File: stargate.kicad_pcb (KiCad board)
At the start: 2 copper layers, 96 x 65.5 mm, 32 parts, among them J1 Mot_Conn, J10 Chev5_conn, J11 Chev6_conn, J12 Chev7_conn, J13 Audio_conn, J14 IOExpander_Conn, J2 Power_Conn, J3 LED_Strip_Conn, J4 DHD_Conn, J5 Level_Converter, J6 Chev1_conn, J7 Chev2_conn, J8 Chev3_conn, J9 Chev4_conn, Q1 PN2222A, Q2 PN2222A, Q3 PN2222A, Q4 PN2222A, Q5 PN2222A, Q6 PN2222A, Q7 PN2222A, U1 ESP32-S3-DevKitC

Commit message: Updates
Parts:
- removed Q1, Q2, Q3, Q4, Q5, Q6, Q7: PN2222A, Package_TO_SOT_THT:TO-92_Inline
- removed R2, R3, R4, R5, R6, R7, R8: 220Ω, Resistor_THT:R_Axial_DIN0204_L3.6mm_D1.6mm_P7.62mm_Horizontal
- added U2: ULN2803A, Package_DIP:DIP-18_W7.62mm, F.Cu at (91.8, 71.9)
- moved J12 54.6 mm to (68.9, 92.2)
- moved J6 53.7 mm to (123.2, 92.2)
- moved J11 36.6 mm to (77.9, 92.2)
- moved J7 35.5 mm to (113.9, 92.2)
- moved J10 18.6 mm to (86.9, 92.2)
- moved J8 17.5 mm to (104.9, 92.2)
- moved J9 1.45 mm to (95.9, 92.2)
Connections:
- U1 pad 1: 3V3 -> unconnected-(U1-3V3-Pad1)
- U1 pad 2: 3V3 -> unconnected-(U1-3V3-Pad1)
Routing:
- net Net-(Q7-B): track 48.3 -> 0.00 mm, vias 2 -> 0
- net Net-(Q6-B): track 38.9 -> 0.00 mm, vias 2 -> 0
- net Net-(Q1-B): track 34.6 -> 0.00 mm
- net Net-(Q5-B): track 31.5 -> 0.00 mm, vias 2 -> 0
- net Net-(J6-Pin_1): track 7.00 -> 36.6 mm
- net Chev1_led: track 42.2 -> 69.1 mm
- net Net-(Q2-B): track 26.9 -> 0.00 mm
- net Net-(Q3-B): track 25.2 -> 0.00 mm
- net Net-(Q4-B): track 24.9 -> 0.00 mm
- net Net-(J7-Pin_1): track 7.00 -> 29.9 mm
- net Chev2_led: track 42.8 -> 65.5 mm
- net 3V3: track 230.9 -> 209.8 mm, vias 2 -> 0
- net Chev3_led: track 43.4 -> 61.9 mm
- net Net-(J8-Pin_1): track 7.00 -> 23.5 mm
- net Chev4_led: track 39.8 -> 54.1 mm
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
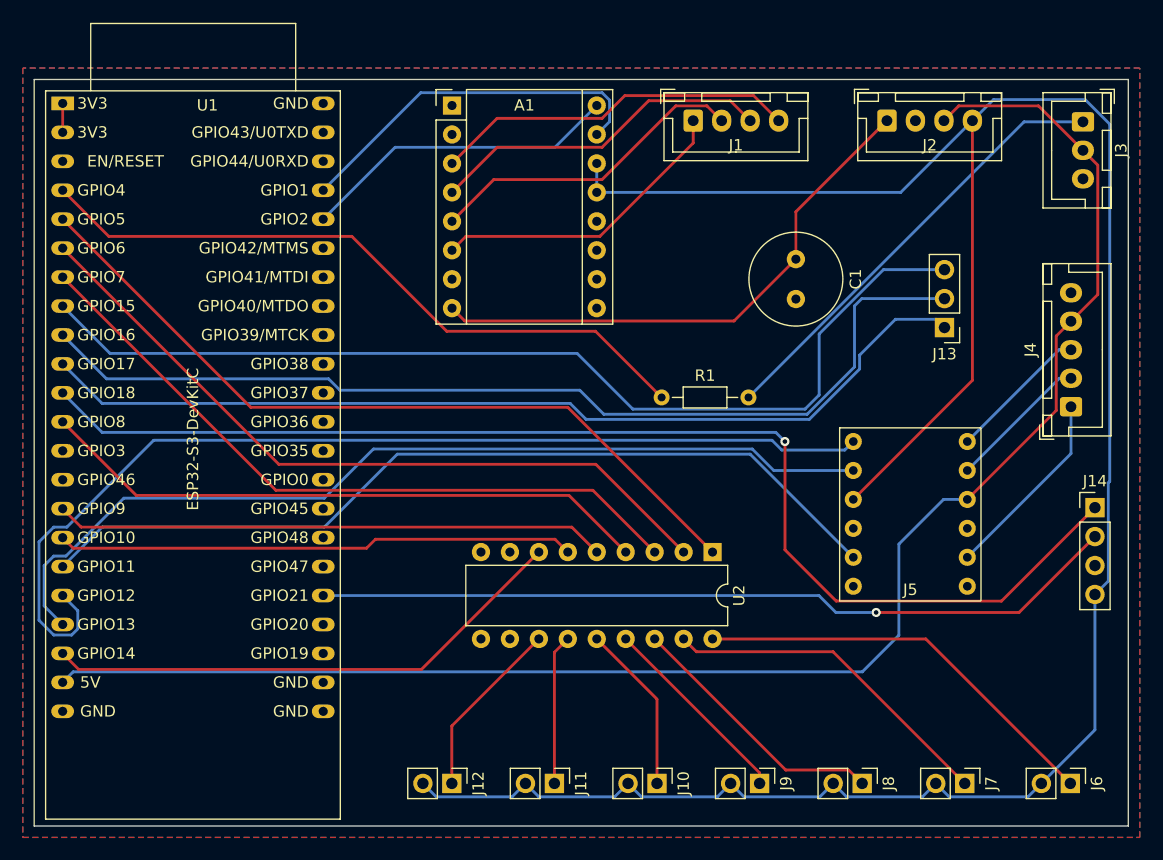
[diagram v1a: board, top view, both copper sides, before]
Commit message: Remove level converter because we'll use usb for the dhd
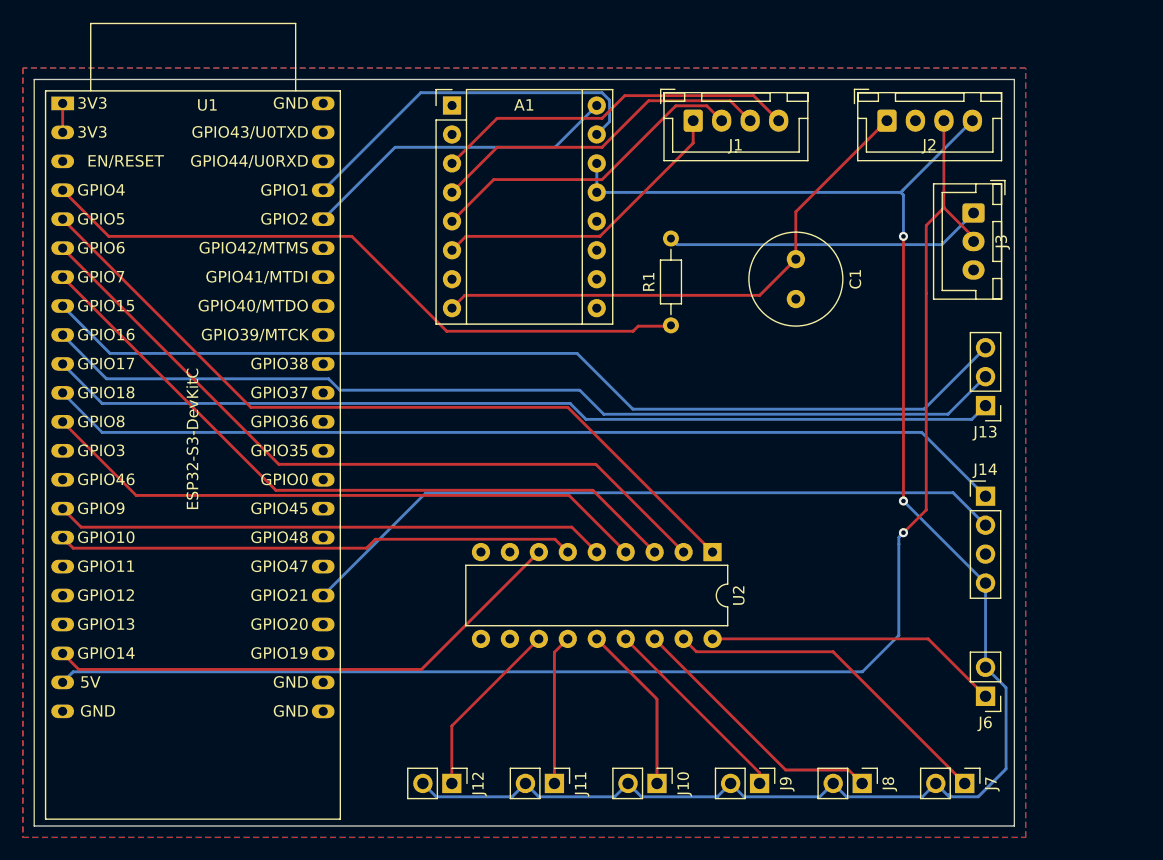
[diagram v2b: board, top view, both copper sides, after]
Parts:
- removed J4: DHD_Conn, Connector_JST:JST_XH_B5B-XH-A_1x05_P2.50mm_Vertical
- removed J5: Level_Converter, Stargate:Level_Converter
- moved J3 12.5 mm to (114.7, 42.2)
- moved J6 10.7 mm to (115.8, 84.6), turned to 180 degrees
- moved J14 9.65 mm to (115.8, 67.0)
- moved J13 7.74 mm to (115.8, 59.1)
- moved R1 6.37 mm to (88.2, 52.0), turned to 90 degrees
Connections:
- U1 pad 17: MOSI -> unconnected-(U1-GPIO11/ADC2_CH0-Pad17)
- U1 pad 18: SCK -> unconnected-(U1-GPIO12/ADC2_CH1-Pad18)
- U1 pad 19: MISO -> unconnected-(U1-GPIO13/ADC2_CH2-Pad19)
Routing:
- net SCK: track 90.3 -> 0.00 mm
- net MISO: track 81.9 -> 0.00 mm
- net MOSI: track 77.2 -> 0.00 mm
- net 3V3: track 209.8 -> 150.4 mm, vias 0 -> 2
- net SCL: track 107.1 -> 84.7 mm, vias 1 -> 0
- net DHD_MISO: track 17.0 -> 0.00 mm
- net 5V: track 141.0 -> 125.9 mm, vias 0 -> 1
- net DHD_MOSI: track 12.5 -> 0.00 mm
- net DHD_SCK: track 12.4 -> 0.00 mm
- net Net-(J3-Pin_1): track 39.4 -> 27.9 mm
- net Net-(J6-Pin_1): track 36.6 -> 26.0 mm
- net SDA: track 71.1 -> 63.0 mm, vias 1 -> 0
- net BCLK: track 87.6 -> 85.2 mm
- net LRC: track 89.3 -> 86.9 mm
- net WS2812B_Data: track 60.1 -> 58.7 mm
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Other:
- board size 96 x 65.5 mm -> 86 x 65.5 mm

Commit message: Disconnected GND from uln2803's COM
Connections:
- U2 pad 10: GND -> unconnected-(U2-COM-Pad10)
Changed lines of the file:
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@@
   (net 60 "unconnected-(U1-GPIO12{slash}ADC2_CH1-Pad18)")
   (net 61 "unconnected-(U1-GPIO13{slash}ADC2_CH2-Pad19)")
+  (net 62 "unconnected-(U2-COM-Pad10)")
   (footprint "Connector_JST:JST_XH_B4B-XH-A_1x04_P2.50mm_Vertical" (layer "F.Cu")
     (at 107.12 34.075732)
@@
       (net 25 "GND") (pinfunction "GND") (pintype "power_in"))
     (pad "10" thru_hole oval (at 7.62 20.32 270) (size 1.6 1.6) (drill 0.8) (layers "*.Cu" "*.Mask")
-      (net 25 "GND") (pinfunction "COM") (pintype "passive"))
+      (net 62 "unconnected-(U2-COM-Pad10)") (pinfunction "COM") (pintype "passive+no_connect"))
     (pad "11" thru_hole oval (at 7.62 17.78 270) (size 1.6 1.6) (drill 0.8) (layers "*.Cu" "*.Mask")
       (net 57 "unconnected-(U2-O8-Pad11)") (pinfunction "O8") (pintype "open_collector"))
